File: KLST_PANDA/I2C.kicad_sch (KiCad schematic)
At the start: 2 parts

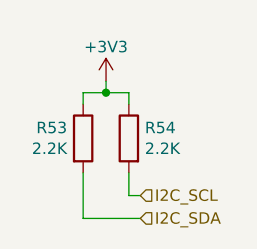
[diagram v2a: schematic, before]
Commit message: started cleaning up schematic ( addressing DRC errors/warning ) (WIP)
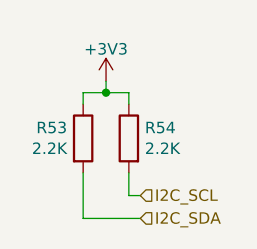
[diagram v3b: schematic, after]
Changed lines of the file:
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@@
       (effects (font (size 1.27 1.27)) hide)
     )
-    (property "Value" "+3V3" (at 143.51 90.17 0)
+    (property "Value" "+3V3" (at 143.51 90.424 0)
       (effects (font (size 1.27 1.27)))
     )
@@
       (project "KLST_PANDA"
         (path "/b4513875-4c57-4720-bcc5-43ead67fe18f/1de475bd-0e17-4802-9721-941bfddbd8b4"
-          (reference "#PWR068") (unit 1)
+          (reference "#PWR069") (unit 1)
         )
       )

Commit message: removed DRC warnings and error, added power page
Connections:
- net +3V3 renamed +3.3V
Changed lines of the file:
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@@
     (stroke (width 0) (type default))
   )
-  (wire (pts (xy 143.51 93.98) (xy 143.51 95.25))
+  (wire (pts (xy 143.51 93.345) (xy 143.51 95.25))
     (stroke (width 0) (type default))
   )
@@
       (project "KLST_PANDA"
         (path "/b4513875-4c57-4720-bcc5-43ead67fe18f/1de475bd-0e17-4802-9721-941bfddbd8b4"
-          (reference "R50") (unit 1)
+          (reference "R36") (unit 1)
         )
       )
     )
   )
-  (symbol (lib_id "power:+3V3") (at 143.51 93.98 0) (unit 1)
-    (in_bom yes) (on_board yes) (dnp no)
-    (property "Reference" "#PWR077" (at 143.51 97.79 0)
+  (symbol (lib_id "power:+3.3V") (at 143.51 93.345 0) (unit 1)
+    (in_bom yes) (on_board yes) (dnp no) (fields_autoplaced)
+    (property "Reference" "#PWR077" (at 143.51 97.155 0)
       (effects (font (size 1.27 1.27)) hide)
     )
-    (property "Value" "+3V3" (at 143.51 90.424 0)
+    (property "Value" "+3.3V" (at 143.51 88.265 0)
       (effects (font (size 1.27 1.27)))
     )
-    (property "Footprint" "" (at 143.51 93.98 0)
+    (property "Footprint" "" (at 143.51 93.345 0)
       (effects (font (size 1.27 1.27)) hide)
     )
-    (property "Datasheet" "" (at 143.51 93.98 0)
+    (property "Datasheet" "" (at 143.51 93.345 0)
       (effects (font (size 1.27 1.27)) hide)
     )
     (pin "1")
     (instances
-      (project "KLST_SHEEP"
-        (path "/7c1fd6fc-5c53-4ccb-a456-46fe6fc0bc71"
+      (project "KLST_PANDA"
+        (path "/b4513875-4c57-4720-bcc5-43ead67fe18f/47e8e77e-c64e-4c44-bfd8-2073580a3d85"
           (reference "#PWR077") (unit 1)
         )
-      )
-      (project "KLST_PANDA"
         (path "/b4513875-4c57-4720-bcc5-43ead67fe18f/1de475bd-0e17-4802-9721-941bfddbd8b4"
-          (reference "#PWR069") (unit 1)
+          (reference "#PWR062") (unit 1)
         )
       )
@@
       (project "KLST_PANDA"
         (path "/b4513875-4c57-4720-bcc5-43ead67fe18f/1de475bd-0e17-4802-9721-941bfddbd8b4"
-          (reference "R51") (unit 1)
+          (reference "R37") (unit 1)
         )
       )
